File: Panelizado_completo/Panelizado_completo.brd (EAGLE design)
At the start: 130 x 50 mm, 1 part

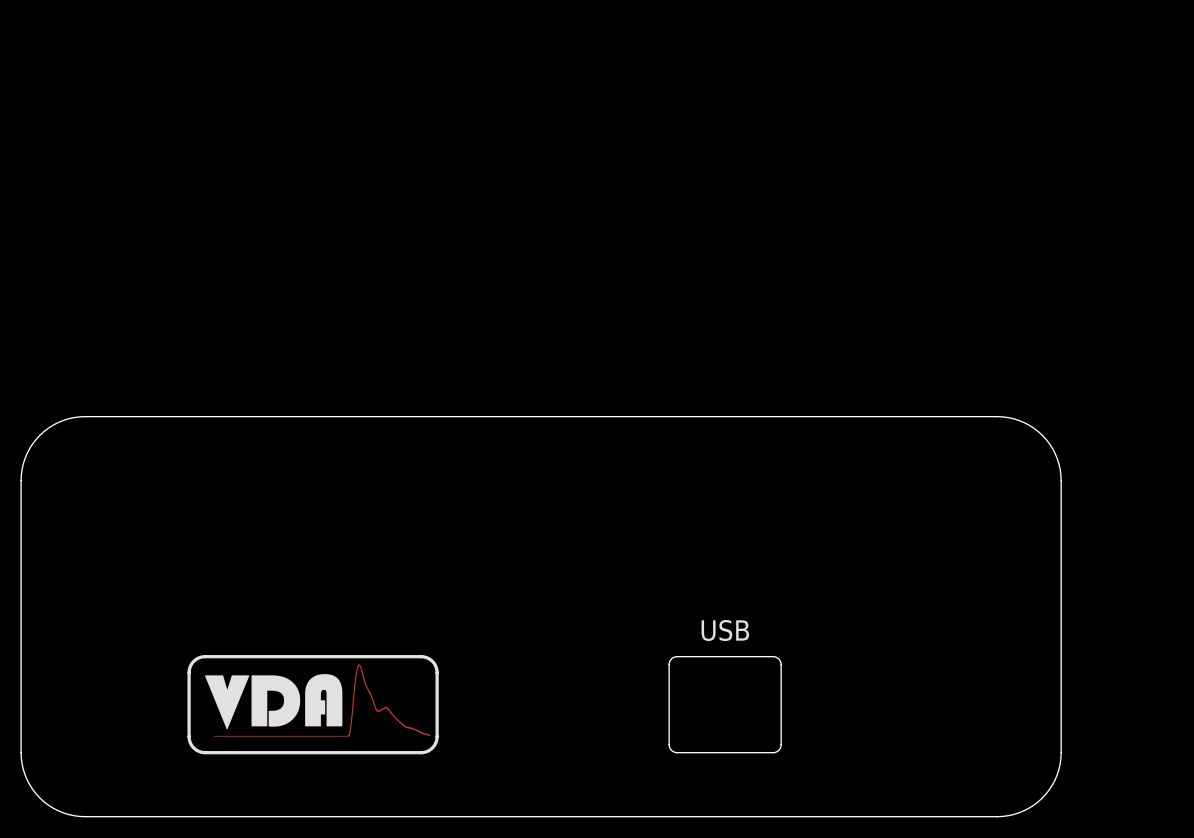
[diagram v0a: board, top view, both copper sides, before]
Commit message: trabajando en los panelizados
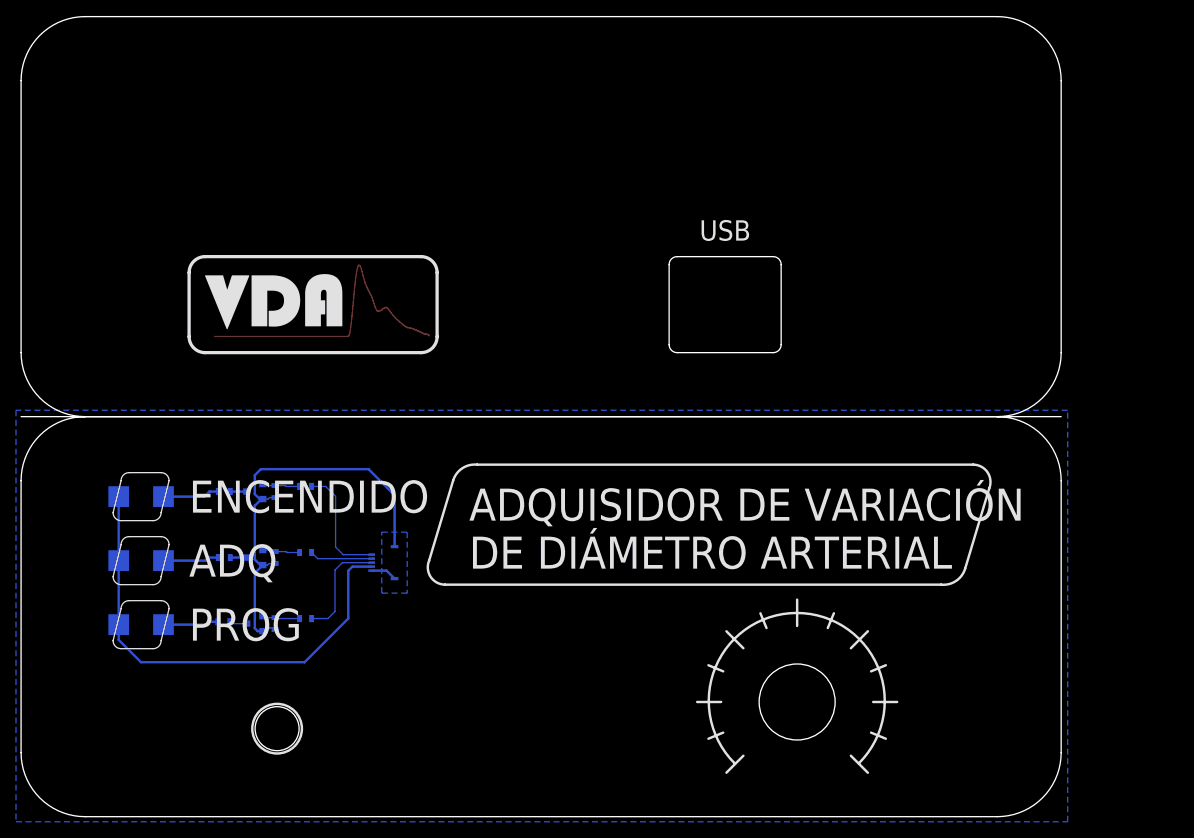
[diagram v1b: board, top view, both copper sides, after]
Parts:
- removed U$2: LOGO_VDA-3CM, Frames:LOGO_VDA-3CM
- added D4, D5, D6: LED-REVERSE_MOUNT, property_LED:VLRK31
- added J2: F0504-H-05-10G-R, property-connectors:F0504-H-05-10G-R
- added Q4, Q5, Q6: BSS138, Property-standar:SOT-23
- added R10, R12, R14: 100K, Property-standar:R_0603
- added R11, R13, R15, R16, R17, R18: 100R, Property-standar:R_0603
- added U$1: LOGO_VDA-3CM, Frames:LOGO_VDA-3CM
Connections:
- new net +3V3: D4.A, D5.A, D6.A, J2.P$4
- new net GND: J2.P$5, J2.P$7, J2.P$8, Q4.2, Q5.2, Q6.2, R10.1, R12.1, R14.1
- new net N$13: Q4.1, R10.2, R11.1
- new net N$14: Q5.1, R12.2, R13.1
- new net N$15: Q6.1, R14.2, R15.1
- new net N$16: J2.P$3, R11.2
- new net N$17: J2.P$2, R13.2
- new net N$18: J2.P$1, R15.2
- new net N$19: D4.K, R16.1
- new net N$20: Q4.3, R16.2
- new net N$21: D5.K, R17.1
- new net N$22: Q5.3, R17.2
- new net N$23: D6.K, R18.1
- new net N$24: Q6.3, R18.2
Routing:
- net +3V3: track 0.00 -> 59.1 mm
- net GND: track 0.00 -> 56.4 mm
- net N$18: track 0.00 -> 14.8 mm
- net N$16: track 0.00 -> 13.4 mm
- net N$17: track 0.00 -> 7.82 mm
- net N$23: track 0.00 -> 7.12 mm
- net N$21: track 0.00 -> 7.01 mm
- net N$19: track 0.00 -> 6.94 mm
- net N$15: track 0.00 -> 4.72 mm
- net N$14: track 0.00 -> 4.72 mm
- net N$13: track 0.00 -> 4.72 mm
- net N$20: track 0.00 -> 2.21 mm
- net N$24: track 0.00 -> 2.06 mm
- net N$22: track 0.00 -> 2.06 mm
- added copper zone on layer 16, net GND
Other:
- board size 130 x 50 mm -> 130 x 100 mm
- board text added: "ADQ"
- board text added: "ADQUISIDOR DE VARIACIÓN DE DIÁMETRO ARTERIAL"
- board text added: "Diseñado por Leandro Zabala"
- board text added: "ENCENDIDO"
- board text added: "PROG"
- board text added: "V-SCORING"
